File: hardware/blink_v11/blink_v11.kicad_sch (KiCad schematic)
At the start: 177 parts, among them J1 Conn_01x02, J14 Conn_02x16_Odd_Even, J15 Conn_01x01, J16 Conn_01x01, J5 Conn_01x06_Pin, J6 Conn_01x03, J7 Conn_01x06_Pin, J9 USB_C_Receptacle, Q3 2N7002, Q4 2N7002, Q5 2N7002, SW1 SW_SPDT, SW2 SW_Push_4PDT, SW3 SW_Push_4PDT, SW4 SW_Push_4PDT, U1 AMS1117-3.3, U10 TMP112AIDRLR, U11 MAX40200AUK, U12 MAX40200AUK, U13 AMS1117-3.3, U14 SN74LVC1G14DBV, U16 TPS63060, U3 M24C02-RMN, U4 STM32F405RGTx, U5 SN74LVC1G14DBV, U6 SN74LVC1G14DBV, U7 CH340C, U8 USBLC6-2P6, U9 MCP73832-2-OT, X1 GTXO-14V (2.048MHz), Y1 16MHz

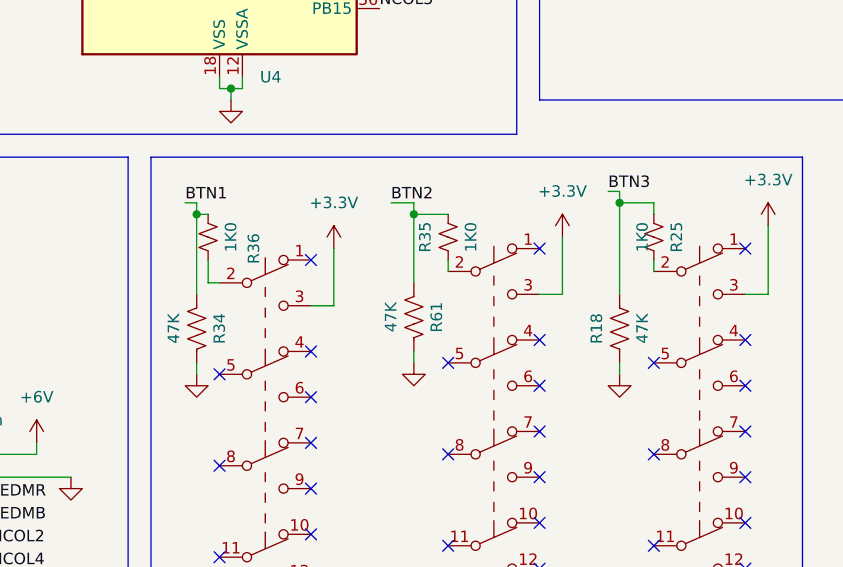
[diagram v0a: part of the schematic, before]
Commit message: remove needless pull down reistors. Fixes #304
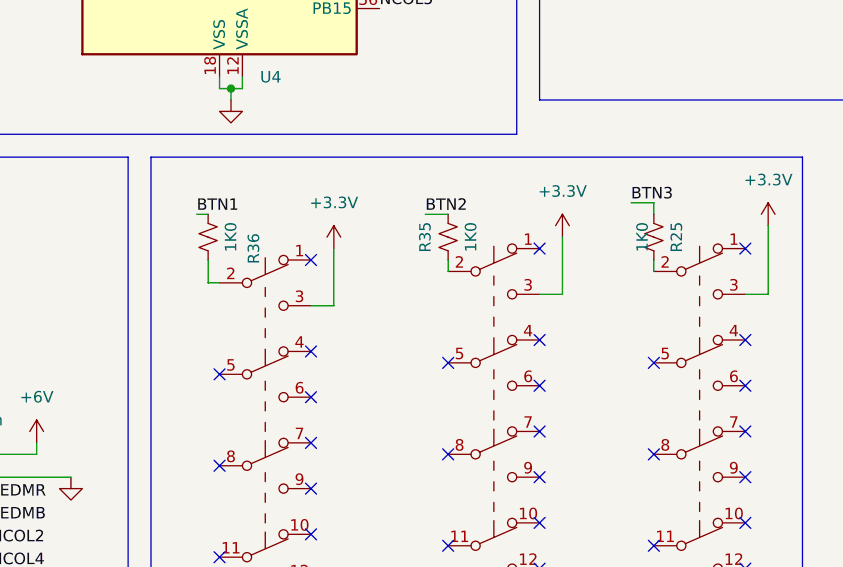
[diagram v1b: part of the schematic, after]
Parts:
- removed R18, R34, R61: 47K, Resistor_SMD:R_0603_1608Metric, symbol Device:R_US

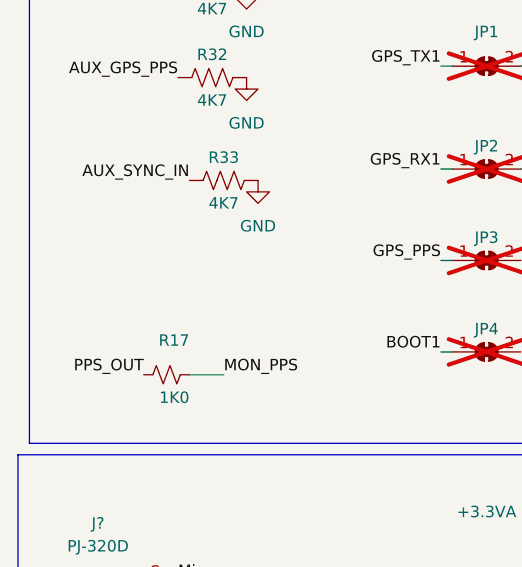
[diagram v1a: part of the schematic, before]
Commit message: start space for battery
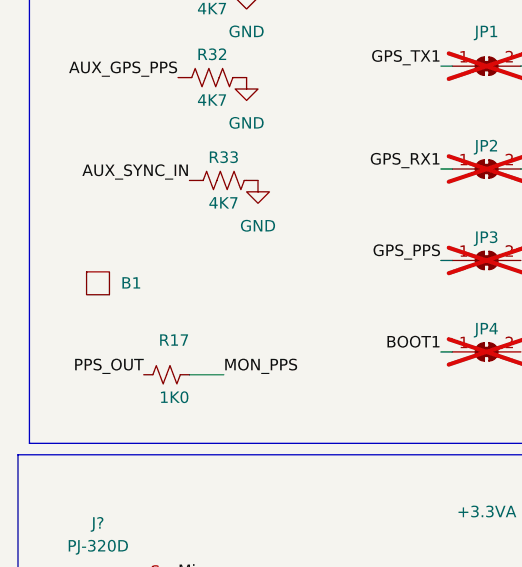
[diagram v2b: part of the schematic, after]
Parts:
- added B1: ~, blinky_footprints:BatteryFlat1, symbol BlinkyShared:Battery
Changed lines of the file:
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@@
+    )
+  )
+  (symbol (lib_id "BlinkyShared:Battery") (at 21.59 170.18 0) (unit 1)
+    (in_bom no) (on_board yes) (dnp no) (fields_autoplaced)
+    (property "Reference" "B1" (at 24.13 170.18 0)
+      (effects (font (size 1.27 1.27)) (justify left))
+    )
+    (property "Value" "~" (at 21.59 170.18 0)
+      (effects (font (size 1.27 1.27)))
+    )
+    (property "Footprint" "blinky_footprints:BatteryFlat1" (at 21.59 170.18 0)
+      (effects (font (size 1.27 1.27)) hide)
+    )
+    (property "Datasheet" "" (at 21.59 170.18 0)
+      (effects (font (size 1.27 1.27)) hide)
+    )
+    (property "Sim.Enable" "0" (at 21.59 170.18 0)
+      (effects (font (size 1.27 1.27)) hide)
+    )
+    (instances
+      (project "blink_v11"
+        (path "/bd4d3b9a-07c1-4a53-9c94-2893f3e869d4"
+          (reference "B1") (unit 1)
+        )
+      )
     )
   )

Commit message: clean up pcb to make more room
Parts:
- removed JP10, JP8: SolderJumper_2_Bridged, Jumper:SolderJumper-2_P1.3mm_Bridged2Bar_RoundedPad1.0x1.5mm, symbol Jumper:SolderJumper_2_Bridged
- removed R14: 47K, Resistor_SMD:R_0603_1608Metric, symbol Device:R_US
- removed S1, S2: 147873-2, SW_147873-2, symbol BlinkyShared:147873-2
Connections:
- net VOUT1 is gone; now on net +6V: C38.1, C39.1, C40.1, R60.1, TP11.1, U16.9 (VOUT)
- net VIN1: now also R62.1, TP13.1

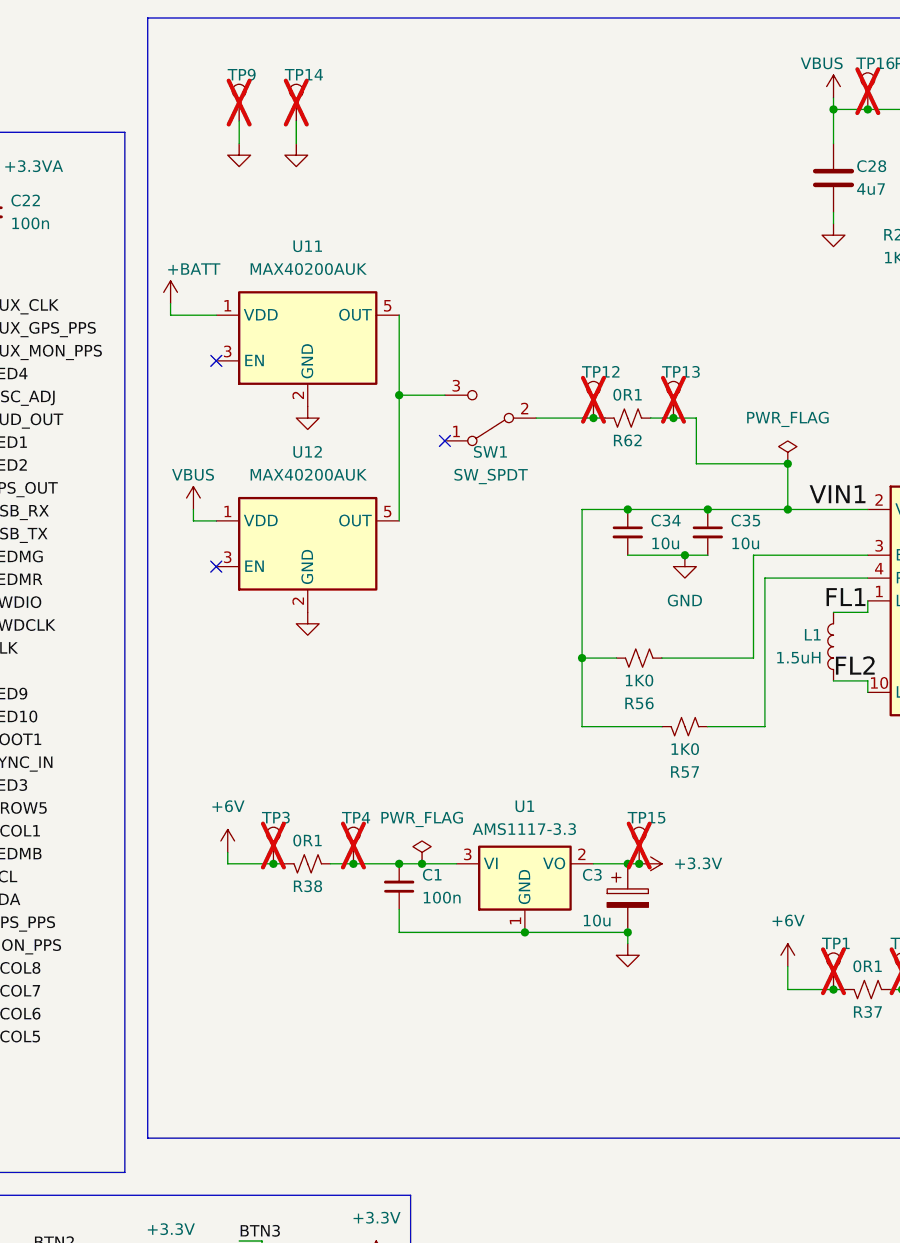
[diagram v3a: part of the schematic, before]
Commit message: start adding battery under voltageprotection  UVP
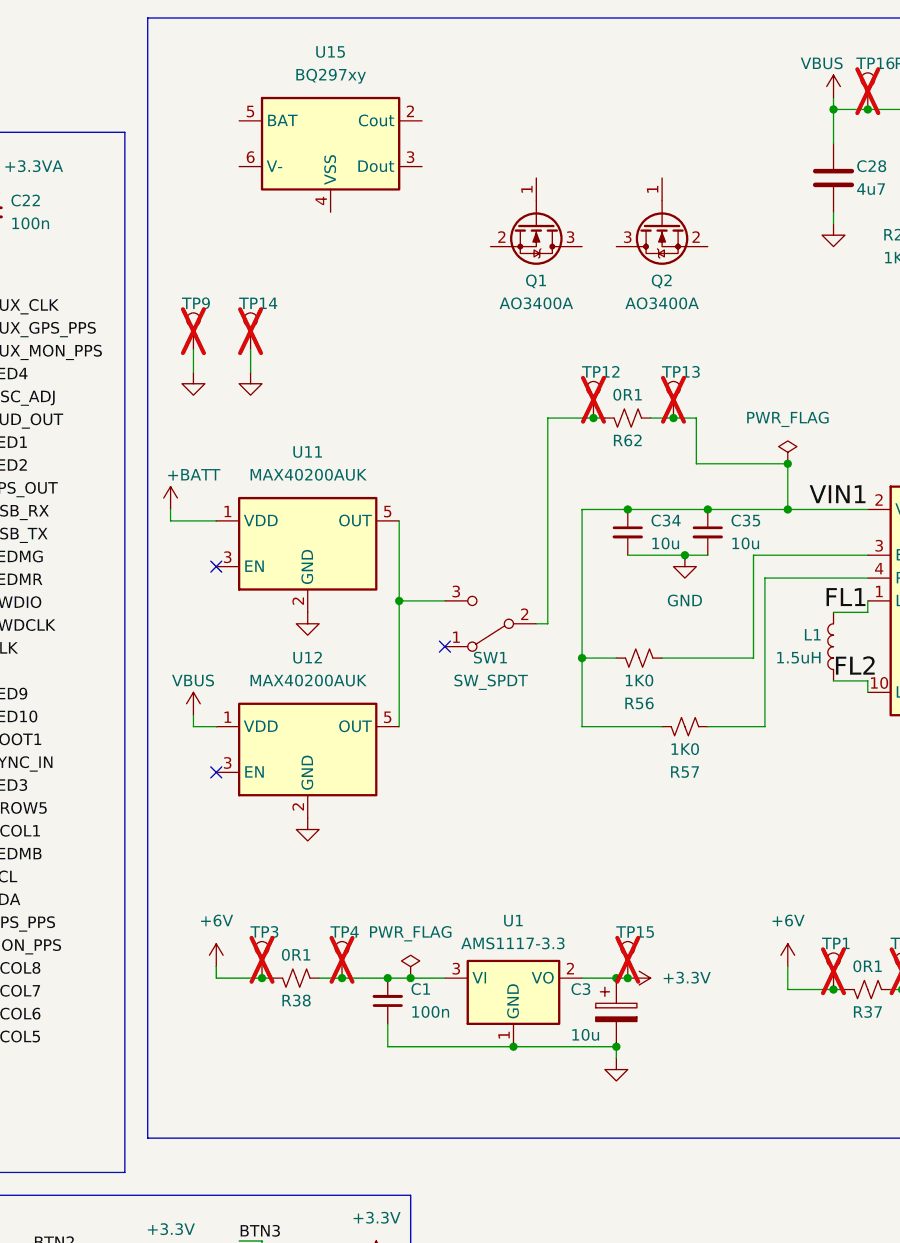
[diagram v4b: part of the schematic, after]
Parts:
- added Q1, Q2: AO3400A, Package_TO_SOT_SMD:SOT-23, symbol Transistor_FET:AO3400A
- added U15: BQ297xy, Package_SON:WSON-6_1.5x1.5mm_P0.5mm, symbol Battery_Management:BQ297xy
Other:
- moved on the sheet: C1, C3, R38, SW1, TP14, TP15, TP3, TP4, TP9, U1, U11, U12

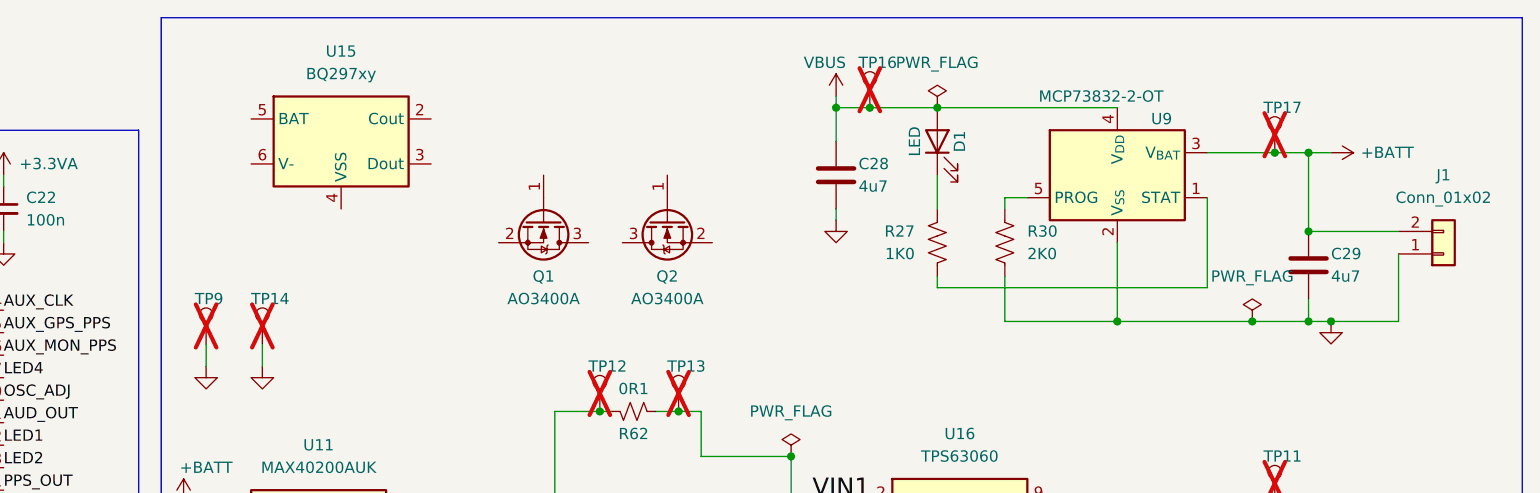
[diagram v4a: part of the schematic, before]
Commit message: clean up for move of cpu
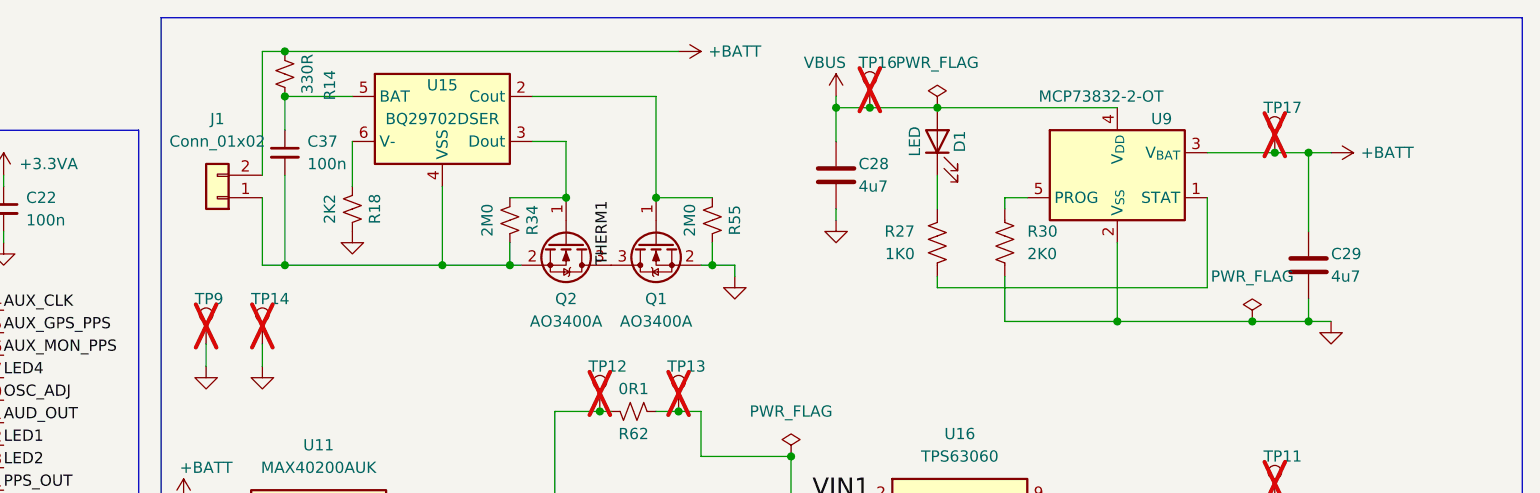
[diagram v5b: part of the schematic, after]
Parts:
- added C37: 100n, Capacitor_SMD:C_0402_1005Metric, symbol Device:C_Small
- added R14: 330R, Resistor_SMD:R_0603_1608Metric, symbol Device:R_Small_US
- added R18: 2K2, Resistor_SMD:R_0603_1608Metric, symbol Device:R_Small_US
- added R34, R55: 2M0, Resistor_SMD:R_0603_1608Metric, symbol Device:R_Small_US
- U15: value BQ297xy -> BQ29702DSER; JLCPCB Part # (none) -> C2872632
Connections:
- net +BATT: now also R14.2
- net GND: now also Q1.2 (S), R18.1, R55.1; no longer J1.1 (Pin_1)
- net at Q1.1 (G): now also U15.2 (Cout), R55.2
- net THERM1: now reaches Q1.3 (D)
- net THERM1: now also Q2.3 (D)
- net at U15.3 (Dout): now also Q2.1 (G), R34.2
- net at U15.4 (VSS): now also J1.1 (Pin_1), Q2.2 (S), C37.2, R34.1
- net at U15.5 (BAT): now also C37.1, R14.1
- net at U15.6 (V-): now also R18.2
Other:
- moved on the sheet: J1, Q1, Q2, U15

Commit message: add test points for battery protection
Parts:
- added TP20, TP21: ~, TestPoint:TestPoint_THTPad_D1.5mm_Drill0.7mm, symbol Connector:TestPoint
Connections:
- net +BATT: now also TP20.1
- net at C37.2, J1.1 (Pin_1), Q2.2 (S)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: now also TP21.1
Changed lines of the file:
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@@
   (title_block
     (title "Blink ")
-    (date "2024-02-17")
+    (date "2024-02-21")
     (rev "V11")
     (company "Cullen Jennings")
@@
   (junction (at 279.4 21.59) (diameter 0) (color 0 0 0 0)
   )
+  (junction (at 280.67 40.64) (diameter 0) (color 0 0 0 0)
+  )
   (junction (at 187.96 34.29) (diameter 0) (color 0 0 0 0)
   )
@@
   (junction (at 181.61 248.92) (diameter 0) (color 0 0 0 0)
   )
+  (junction (at 276.86 21.59) (diameter 0) (color 0 0 0 0)
+  )
   (junction (at 393.7 67.31) (diameter 0) (color 0 0 0 0)
   )
@@
     (stroke (width 0) (type default))
   )
-  (wire (pts (xy 279.4 40.64) (xy 297.18 40.64))
+  (wire (pts (xy 279.4 40.64) (xy 280.67 40.64))
     (stroke (width 0) (type default))
   )
@@
     (stroke (width 0) (type default))
   )
+  (wire (pts (xy 274.32 21.59) (xy 276.86 21.59))
+    (stroke (width 0) (type default))
+  )
   (wire (pts (xy 195.58 111.76) (xy 212.09 111.76))
     (stroke (width 0) (type default))
@@
     (stroke (width 0) (type default))
   )
+  (wire (pts (xy 276.86 21.59) (xy 276.86 30.48))
+    (stroke (width 0) (type default))
+  )
   (wire (pts (xy 360.68 41.91) (xy 360.68 46.99))
     (stroke (width 0) (type default))
@@
     (stroke (width 0) (type default))
   )
+  (wire (pts (xy 280.67 40.64) (xy 297.18 40.64))
+    (stroke (width 0) (type default))
+  )
   (wire (pts (xy 341.63 120.65) (xy 342.9 120.65))
     (stroke (width 0) (type default))
@@
     (stroke (width 0) (type default))
   )
-  (wire (pts (xy 276.86 16.51) (xy 276.86 30.48))
+  (wire (pts (xy 276.86 16.51) (xy 276.86 21.59))
     (stroke (width 0) (type default))
   )
@@
     )
   )
+  (symbol (lib_id "Connector:TestPoint") (at 280.67 40.64 0) (unit 1)
+    (in_bom no) (on_board yes) (dnp yes)
+    (property "Reference" "TP21" (at 278.13 35.56 0)
+      (effects (font (size 1.27 1.27)) (justify left))
+    )
+    (property "Value" "~" (at 279.4 34.29 0)
+      (effects (font (size 1.27 1.27)) (justify left))
+    )
+    (property "Footprint" "TestPoint:TestPoint_THTPad_D1.5mm_Drill0.7mm" (at 285.75 40.64 0)
+      (effects (font (size 1.27 1.27)) hide)
+    )
+    (property "Datasheet" "~" (at 285.75 40.64 0)
+      (effects (font (size 1.27 1.27)) hide)
+    )
+    (pin "1")
+    (instances
+      (project "blink_v11"
+        (path "/bd4d3b9a-07c1-4a53-9c94-2893f3e869d4"
+          (reference "TP21") (unit 1)
+        )
+      )
+    )
+  )
   (symbol (lib_id "power:PWR_FLAG") (at 294.64 119.38 0) (unit 1)
     (in_bom yes) (on_board yes) (dnp no) (fields_autoplaced)
@@
         )
       )
+    )
+  )
+  (symbol (lib_id "Connector:TestPoint") (at 274.32 21.59 0) (unit 1)
+    (in_bom no) (on_board yes) (dnp yes)
+    (property "Reference" "TP20" (at 270.51 16.51 0)
+      (effects (font (size 1.27 1.27)) (justify left))
+    )
+    (property "Value" "~" (at 273.05 15.24 0)
+      (effects (font (size 1.27 1.27)) (justify left))
+    )
+    (property "Footprint" "TestPoint:TestPoint_THTPad_D1.5mm_Drill0.7mm" (at 279.4 21.59 0)
+      (effects (font (size 1.27 1.27)) hide)
+    )
+    (property "Datasheet" "~" (at 279.4 21.59 0)
+      (effects (font (size 1.27 1.27)) hide)
+    )
+    (pin "1")
+    (instances
+      (project "blink_v11"
+        (path "/bd4d3b9a-07c1-4a53-9c94-2893f3e869d4"
+          (reference "TP20") (unit 1)
+        )
+      )
